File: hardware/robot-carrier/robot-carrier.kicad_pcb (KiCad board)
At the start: 2 copper layers, 60 x 73.5 mm, 34 parts, among them J1 DB128L BAT IN, LCSC C500021, J10 M1, J11 M2, J12 M3, J13 M4, J2 DB128L 2P, LCSC C500021, J20 S1, J21 S2, J22 S3, J23 S4, J3 DB128L 2P, LCSC C500021, J30 WT901 UART, J40 GA25-370 L298N: ENA / IN1 / I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, J41 DB128L 3P, LCSC C430602

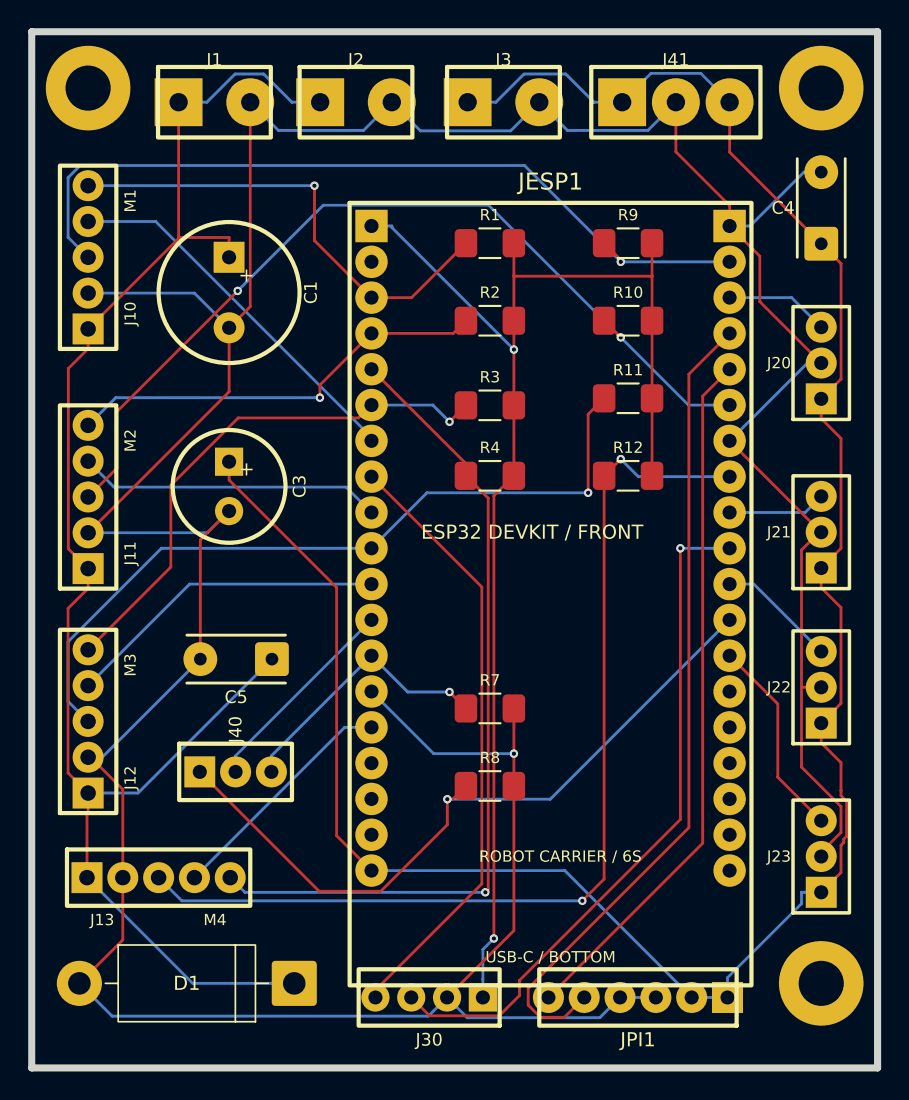
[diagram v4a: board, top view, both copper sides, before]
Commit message: Replace autorouted power trees with copper planes
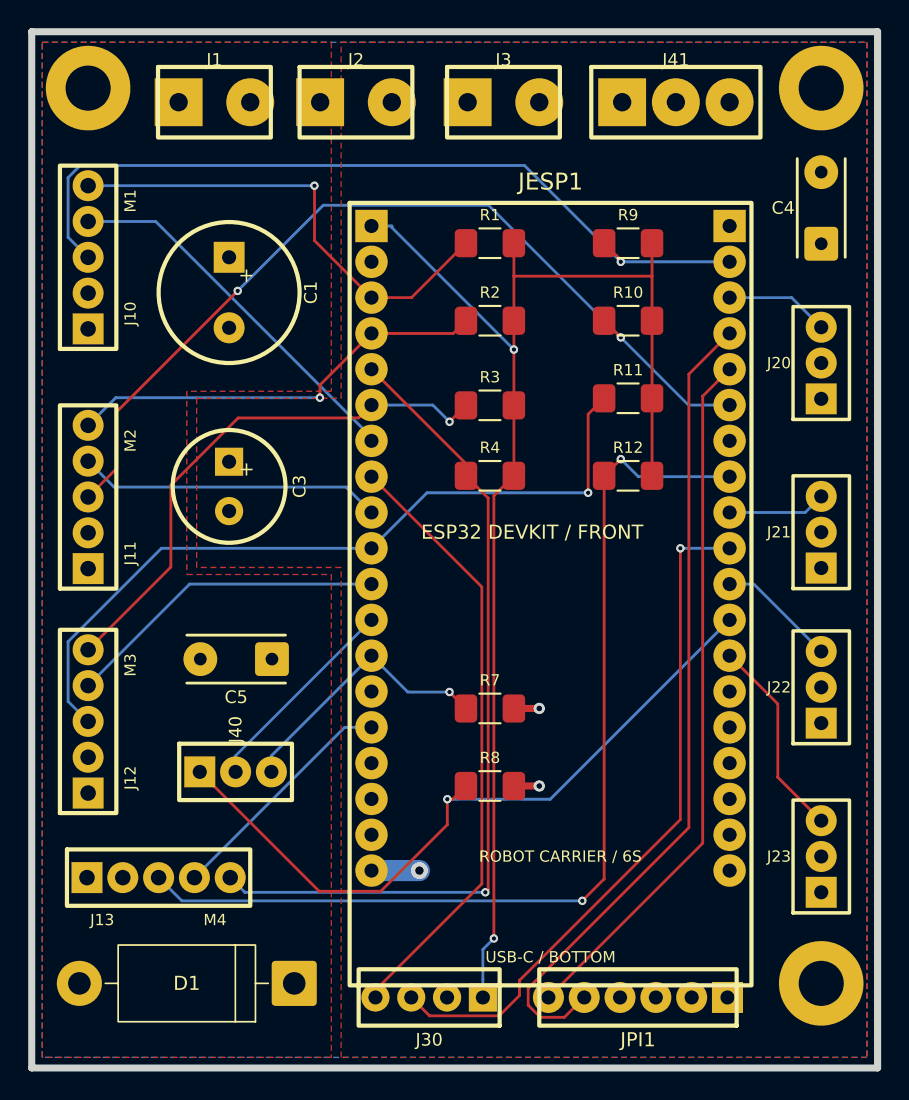
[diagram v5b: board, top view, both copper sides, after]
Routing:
- net GND: track 286.3 -> 3.60 mm, vias 1 -> 2
- net +5V: track 158.8 -> 3.40 mm, vias 0 -> 1
- net VIN_PROTECTED: track 111.5 -> 0.00 mm
- added copper zone on F.Cu, net +5V
- added copper zone on B.Cu, net GND
- added copper zone on F.Cu, net VIN_PROTECTED

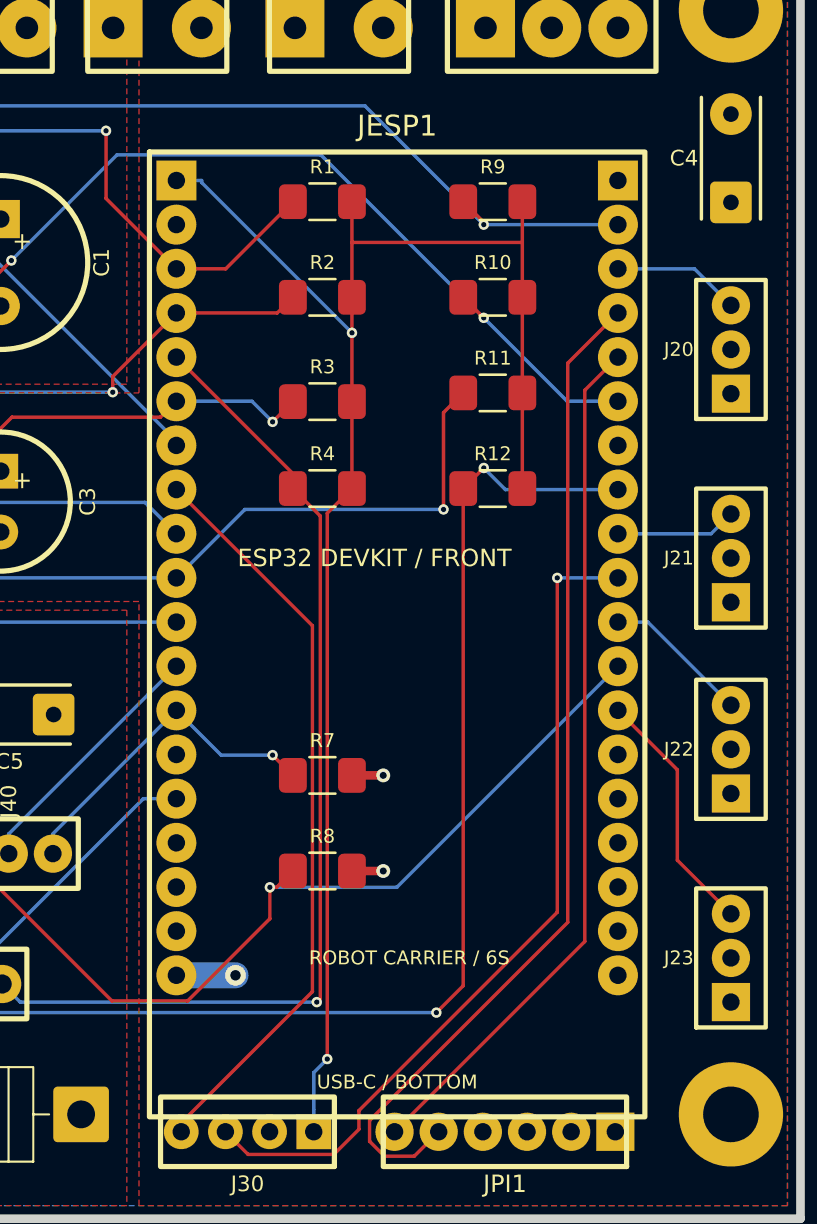
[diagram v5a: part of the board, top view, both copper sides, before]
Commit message: Adapt carrier for 30-pin ESP32 DevKit
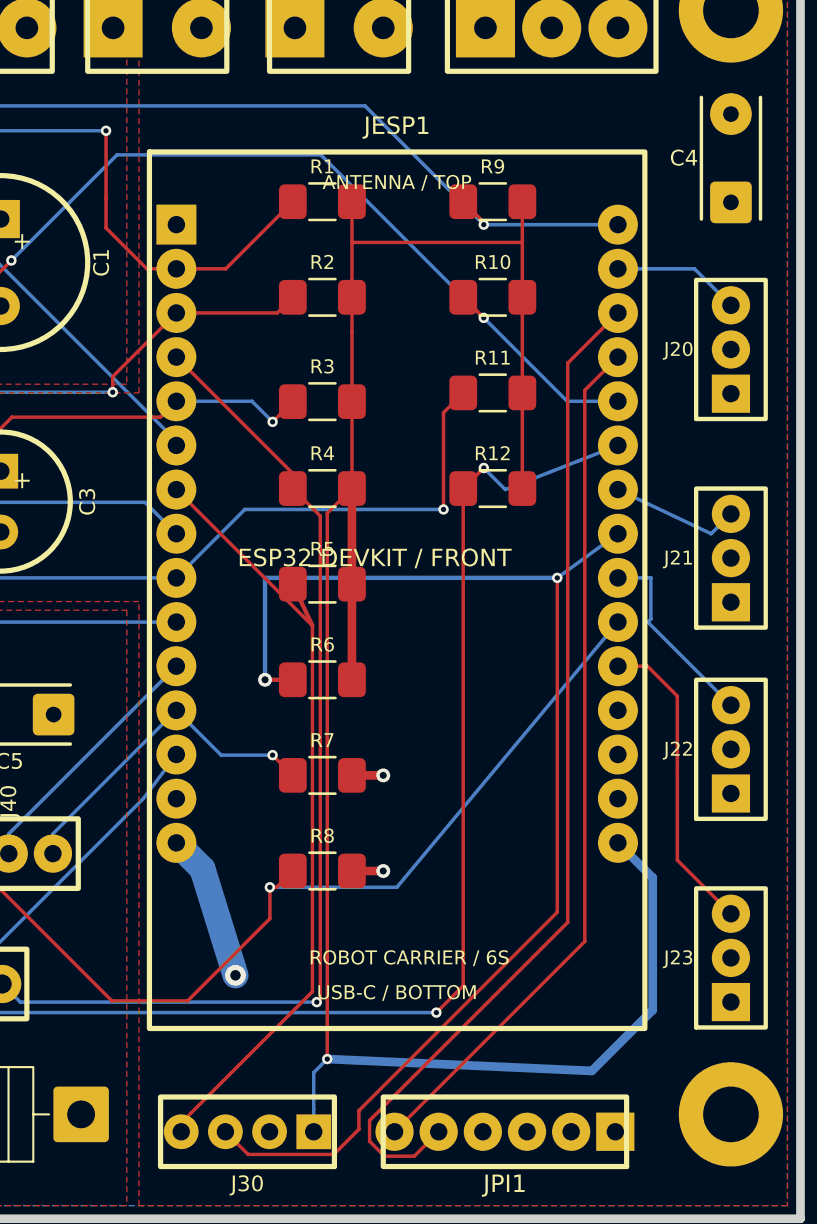
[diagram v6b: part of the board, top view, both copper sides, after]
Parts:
- added R5: 4.7k DNP I2C SDA pull-up, Custom:R_1206_HAND, F.Cu at (52.5, 57.0)
- added R6: 4.7k DNP I2C SCL pull-up, Custom:R_1206_HAND, F.Cu at (52.5, 62.5)
- J30: value WT901 UART -> IMU I2C
- JESP1: value 2x Dupont female 1x19, 38-pin ESP32 DevKitC -> ESP32 DEVKIT V1 30PIN TYPE-C; footprint Custom:ESP32_DEVKITC_38PIN_SOCKET -> ESP32_DEVKIT_V1_30PIN_SOCKET
- moved JESP1 2.54 mm to (56.8, 54.1)
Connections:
- J30 pad 3: IMU_UART_TX_3V3 -> IMU_I2C_SCL_3V3
- J30 pad 4: IMU_UART_RX_3V3 -> IMU_I2C_SDA_3V3
- JESP1 pad 1: +3V3 -> (no net)
- JESP1 pad 10: M3_PWM_3V3 -> M3_DIR_3V3
- JESP1 pad 11: M3_DIR_3V3 -> GA25_IN1_3V3
- JESP1 pad 12: GA25_IN1_3V3 -> GA25_IN2_3V3
- JESP1 pad 13: GA25_IN2_3V3 -> M4_DIR_3V3
- JESP1 pad 15: M4_DIR_3V3 -> +5V
- JESP1 pad 16: (no net) -> M1_PWM_3V3
- JESP1 pad 17: (no net) -> S1_PWM
- JESP1 pad 18: (no net) -> PI_UART_TX_3V3
- JESP1 pad 19: +5V -> PI_UART_RX_3V3
- JESP1 pad 2: (no net) -> M1_ENC
- JESP1 pad 20: GND -> M2_PWM_3V3
- JESP1 pad 21: M1_PWM_3V3 -> M4_PWM_3V3
- JESP1 pad 22: S1_PWM -> S2_PWM
- JESP1 pad 23: PI_UART_TX_3V3 -> IMU_I2C_SCL_3V3
- JESP1 pad 24: PI_UART_RX_3V3 -> S3_PWM
- JESP1 pad 25: M2_PWM_3V3 -> GA25_ENA_PWM_3V3
- JESP1 pad 26: GND -> S4_PWM
- JESP1 pad 27: M4_PWM_3V3 -> (no net)
- JESP1 pad 28: S2_PWM -> (no net)
- JESP1 pad 29: IMU_UART_TX_3V3 -> GND
- JESP1 pad 3: M1_ENC -> M2_ENC
- JESP1 pad 30: S3_PWM -> +3V3
- JESP1 pad 4: M2_ENC -> M4_ENC
- JESP1 pad 5: M4_ENC -> M3_ENC
- JESP1 pad 6: M3_ENC -> M1_DIR_3V3
- JESP1 pad 7: M1_DIR_3V3 -> IMU_I2C_SDA_3V3
- JESP1 pad 8: IMU_UART_RX_3V3 -> M2_DIR_3V3
- JESP1 pad 9: M2_DIR_3V3 -> M3_PWM_3V3
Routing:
- net IMU_I2C_SCL_3V3: track 0.00 -> 73.8 mm, vias 0 -> 2
- net IMU_UART_TX_3V3: track 48.8 -> 0.00 mm, vias 1 -> 0
- net IMU_I2C_SDA_3V3: track 0.00 -> 45.9 mm
- net IMU_UART_RX_3V3: track 43.3 -> 0.00 mm
- net +3V3: track 94.5 -> 122.3 mm, vias 2 -> 1
- net +5V: track 3.40 -> 8.53 mm
- net S4_PWM: track 14.4 -> 17.9 mm
- net S3_PWM: track 8.48 -> 11.3 mm
- net GA25_ENA_PWM_3V3: track 51.8 -> 53.7 mm
- net M4_DIR_3V3: track 17.0 -> 18.2 mm
- net M1_ENC: track 34.0 -> 35.0 mm
- net S2_PWM: track 6.97 -> 7.54 mm

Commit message: updated
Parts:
- C3: value 1000uF 10V, LCSC C79119 -> 1000uF 16V, LCSC C51934166
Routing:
- net +3V3: track 122.3 -> 123.4 mm
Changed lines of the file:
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@@
 			)
 		)
-		(property "Value" "1000uF 10V, LCSC C79119"
+		(property "Value" "1000uF 16V, LCSC C51934166"
 			(at 0 5 90)
 			(layer "F.Fab")
@@
 			)
 		)
-		(property "LCSC" "C79119"
+		(property "LCSC" "C51934166"
 			(at 0 0 90)
 			(layer "F.Fab")
@@
 		(at 56 68)
 		(size 0.8)
-		(drill 0.4)
+		(drill 0.5)
 		(layers "F.Cu" "B.Cu")
 		(net "GND")
@@
 		(at 56 73.5)
 		(size 0.8)
-		(drill 0.4)
+		(drill 0.5)
 		(layers "F.Cu" "B.Cu")
 		(net "GND")
@@
 	(segment
 		(start 59.4669 47.1331)
-		(end 59.4669 52.7035)
+		(end 59.38 52.8)
 		(width 0.2)
 		(layer "F.Cu")
@@
 	)
 	(via
-		(at 59.4669 52.7035)
-		(size 0.6)
-		(drill 0.3)
+		(at 59.38 52.8)
+		(size 0.8)
+		(drill 0.5)
 		(layers "F.Cu" "B.Cu")
 		(net "M3_PWM_3V3")
 	)
 	(segment
-		(start 59.4669 52.7035)
+		(start 59.38 52.8)
 		(end 48.0365 52.7035)
 		(width 0.2)
@@
 	(segment
 		(start 52.7793 84.3173)
-		(end 52.7793 52.9207)
+		(end 52.7793 81.9)
 		(width 0.2)
 		(layer "F.Cu")
@@
 	)
 	(segment
+		(start 53.5 81.7)
+		(end 53.5 80)
+		(width 0.2)
+		(layer "F.Cu")
+		(net "+3V3")
+	)
+	(segment
 		(start 64 37.3428)
 		(end 64 35)
@@
 		(start 54.2 46.5)
 		(end 54.2 51.5)
+		(width 0.2)
+		(layer "F.Cu")
+		(net "+3V3")
+	)
+	(segment
+		(start 52.7793 79.8)
+		(end 52.7793 52.9207)
 		(width 0.2)
 		(layer "F.Cu")
@@
 		(net "+3V3")
 	)
+	(segment
+		(start 53.5 80)
+		(end 52.7793 79.8)
+		(width 0.2)
+		(layer "F.Cu")
+		(net "+3V3")
+	)
+	(segment
+		(start 52.7793 81.9)
+		(end 53.5 81.7)
+		(width 0.2)
+		(layer "F.Cu")
+		(net "+3V3")
+	)
 	(via
 		(at 52.7793 84.3173)
-		(size 0.6)
-		(drill 0.3)
+		(size 0.8)
+		(drill 0.5)
 		(layers "F.Cu" "B.Cu")
 		(net "+3V3")
@@
 	(via
 		(at 40.0545 30.92)
-		(size 0.6)
-		(drill 0.3)
+		(size 0.8)
+		(drill 0.5)
 		(layers "F.Cu" "B.Cu")
 		(net "M1_ENC")
@@
 	(segment
 		(start 66.0101 75.8725)
-		(end 66.0101 56.64)
+		(end 65.9 56.64)
 		(width 0.2)
 		(layer "F.Cu")
@@
 	)
 	(via
-		(at 66.0101 56.64)
-		(size 0.6)
-		(drill 0.3)
+		(at 65.9 56.64)
+		(size 0.8)
+		(drill 0.5)
 		(layers "F.Cu" "B.Cu")
 		(net "IMU_I2C_SCL_3V3")
@@
 		(at 49.2 62.5)
 		(size 0.8)
-		(drill 0.4)
+		(drill 0.5)
 		(layers "F.Cu" "B.Cu")
 		(net "IMU_I2C_SCL_3V3")
@@
 	(segment
 		(start 69.5 54.1)
-		(end 66.0101 56.64)
+		(end 65.9 56.64)
 		(width 0.2)
 		(layer "B.Cu")
@@
 	(via
 		(at 59.0548 81.6448)
-		(size 0.6)
-		(drill 0.3)
+		(size 0.8)
+		(drill 0.5)
 		(layers "F.Cu" "B.Cu")
 		(net "M4_PWM_3V3")
@@
 	(via
 		(at 61.7828 50.3172)
-		(size 0.6)
-		(drill 0.3)
+		(size 0.8)
+		(drill 0.5)
 		(layers "F.Cu" "B.Cu")
 		(net "M4_PWM_3V3")
@@
 	(segment
 		(start 52.3775 80.8404)
-		(end 52.1754 81.0425)
+		(end 52.63 80.84)
 		(width 0.2)
 		(layer "F.Cu")
@@
 	)
 	(via
-		(at 52.1754 81.0425)
-		(size 0.6)
-		(drill 0.3)
+		(at 52.63 80.84)
+		(size 0.8)
+		(drill 0.5)
 		(layers "F.Cu" "B.Cu")
 		(net "M4_ENC")
@@
 	(segment
 		(start 35.1225 81.0425)
-		(end 52.1754 81.0425)
+		(end 52.63 80.84)
 		(width 0.2)
 		(layer "B.Cu")
@@
 	(via
 		(at 61.7817 36.32)
-		(size 0.6)
-		(drill 0.3)
+		(size 0.8)
+		(drill 0.5)
 		(layers "F.Cu" "B.Cu")
 		(net "M1_PWM_3V3")
@@
 	(segment
 		(start 40.4403 45.0597)
-		(end 40.4403 45.9586)
+		(end 40.36 46.04)
 		(width 0.2)
 		(layer "F.Cu")
@@
 	)
 	(via
-		(at 40.4403 45.9586)
-		(size 0.6)
-		(drill 0.3)
+		(at 40.36 46.04)
+		(size 0.8)
+		(drill 0.5)
 		(layers "F.Cu" "B.Cu")
 		(net "M2_ENC")
@@
 	)
 	(segment
-		(start 40.4403 45.9586)
+		(start 40.36 46.04)
 		(end 25.9614 45.9586)
 		(width 0.2)
@@
 	(via
 		(at 49.6357 47.6643)
-		(size 0.6)
-		(drill 0.3)
+		(size 0.8)
+		(drill 0.5)
 		(layers "F.Cu" "B.Cu")
 		(net "M3_ENC")
@@
 	(via
 		(at 49.6346 66.8346)
-		(size 0.6)
-		(drill 0.3)
+		(size 0.8)
+		(drill 0.5)
 		(layers "F.Cu" "B.Cu")
 		(net "GA25_IN2_3V3")
@@
 	)
 	(segment
-		(start 34.6088 38.3821)
+		(start 34.69 38.3)
 		(end 26.0472 46.9437)
 		(width 0.2)
@@
 	(via
 		(at 61.7809 41.6809)
-		(size 0.6)
-		(drill 0.3)
+		(size 0.8)
+		(drill 0.5)
 		(layers "F.Cu" "B.Cu")
 		(net "M2_PWM_3V3")
 	)
 	(via
-		(at 34.6088 38.3821)
-		(size 0.6)
-		(drill 0.3)
+		(at 34.69 38.3)
+		(size 0.8)
+		(drill 0.5)
 		(layers "F.Cu" "B.Cu")
 		(net "M2_PWM_3V3")
@@
 	)
 	(segment
-		(start 34.6088 38.3821)
+		(start 34.69 38.3)
 		(end 40.6832 32.3077)
 		(width 0.2)
@@
 	(via
 		(at 49.4783 74.438)
-		(size 0.6)
-		(drill 0.3)
+		(size 0.8)
+		(drill 0.5)
 		(layers "F.Cu" "B.Cu")
 		(net "GA25_ENA_PWM_3V3")

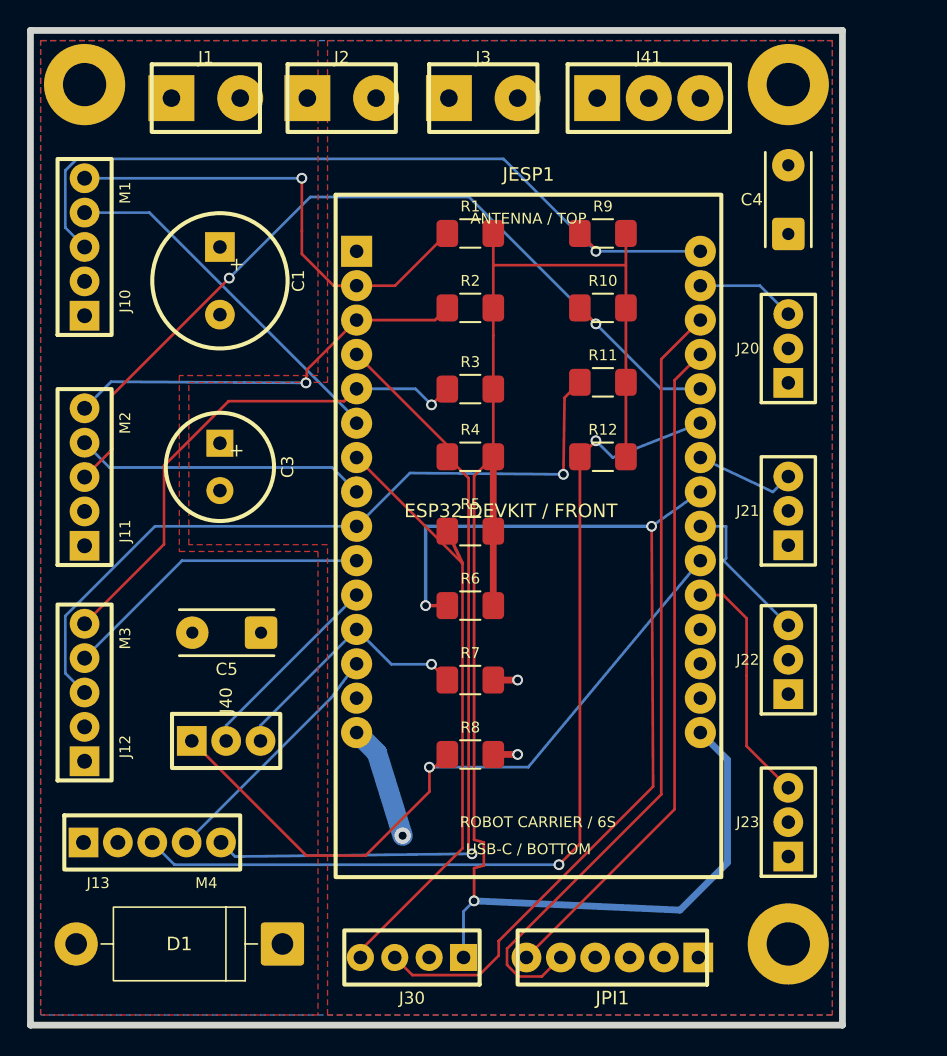
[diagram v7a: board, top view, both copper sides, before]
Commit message: Use 2200uF
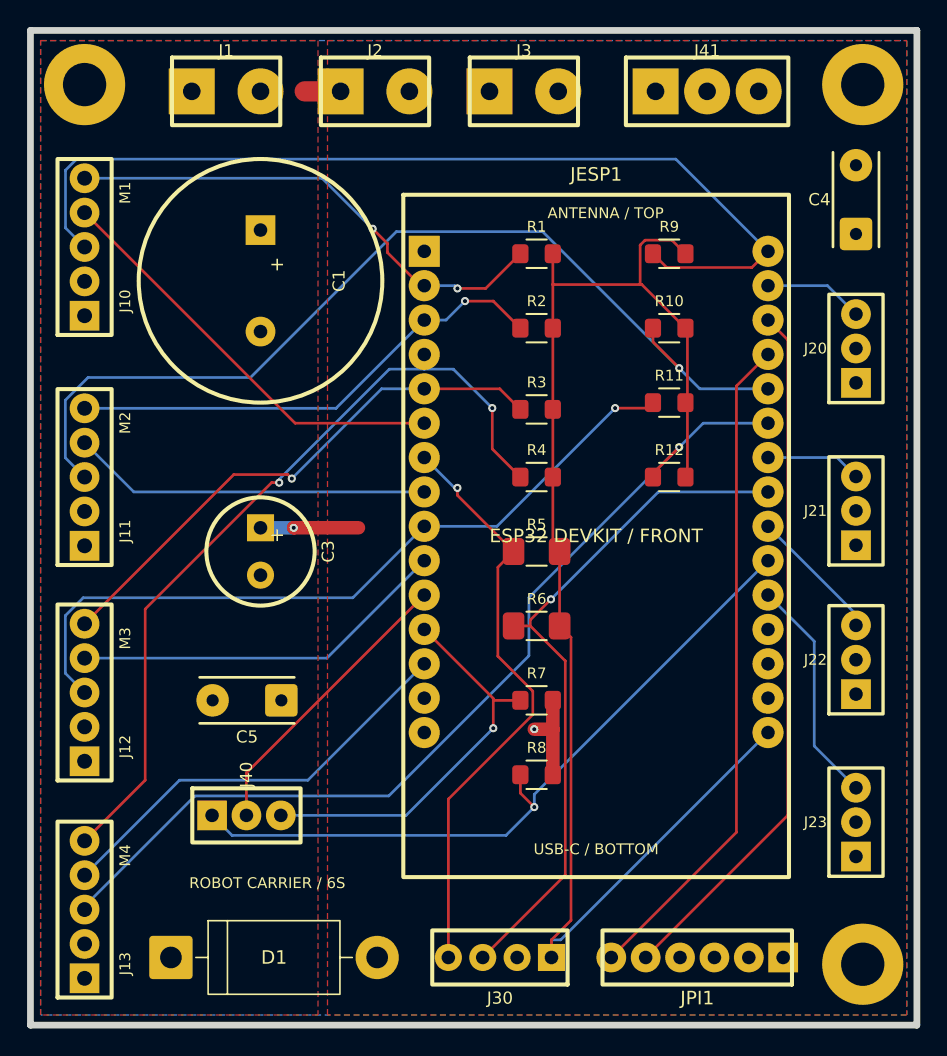
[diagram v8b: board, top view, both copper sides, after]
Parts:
- C1: value 470uF 63V, LCSC C51953331 -> HRK 2200uF 63V CD288, LCSC C2960335; footprint Capacitor_THT:CP_Radial_D10.0mm_P5.00mm -> Capacitor_THT:CP_Radial_D18.0mm_P7.50mm
- R1, R10, R11, R12, R2, R3, R4, R7, R8, R9: footprint Custom:R_1206_HAND -> Custom:R_0805_HAND
- moved D1 8.30 mm to (30.4, 88.5), turned to 0 degrees
- moved J13 7.04 mm to (24.0, 85.0), turned to 90 degrees
- moved C3 6.93 mm to (37.0, 58.5)
- moved J30 6.50 mm to (54.7, 88.5)
- moved JPI1 6.27 mm to (69.3, 88.5)
- moved H3 5.70 mm to (81.5, 89.0)
- moved J40 5.70 mm to (36.0, 78.0)
- moved H2 5.50 mm to (81.5, 24.0)
- moved C5 5.22 mm to (36.0, 69.5)
- moved R10 5.12 mm to (67.2, 42.0)
- moved R11 5.12 mm to (67.2, 47.5)
- moved R12 5.12 mm to (67.2, 53.0)
- moved R9 5.12 mm to (67.2, 36.5)
- moved R1 5.12 mm to (57.4, 36.5)
- moved R2 5.12 mm to (57.4, 42.0)
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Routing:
- net IMU_I2C_SCL_3V3: track 73.9 -> 51.3 mm, vias 2 -> 1
- net +3V3: track 123.4 -> 106.0 mm, vias 1 -> 0
- net M4_DIR_3V3: track 18.2 -> 31.6 mm
- net M1_PWM_3V3: track 58.2 -> 70.7 mm, vias 1 -> 0
- net GA25_IN2_3V3: track 19.4 -> 29.8 mm
- net M2_PWM_3V3: track 64.0 -> 71.9 mm, vias 2 -> 1
- net GA25_IN1_3V3: track 14.8 -> 21.7 mm
- net PI_UART_TX_3V3: track 58.5 -> 52.1 mm
- net M2_ENC: track 30.4 -> 36.3 mm
- net M2_DIR_3V3: track 21.6 -> 26.6 mm
- net M3_DIR_3V3: track 23.1 -> 28.1 mm
- net M1_DIR_3V3: track 26.7 -> 31.5 mm
- net GND: track 3.60 -> 6.87 mm, vias 2 -> 1
- net VIN_PROTECTED: track 0.00 -> 2.65 mm
- net M1_ENC: track 35.0 -> 37.0 mm, vias 1 -> 2
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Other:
- board size 60 x 73.5 mm -> 65.5 x 73.5 mm
